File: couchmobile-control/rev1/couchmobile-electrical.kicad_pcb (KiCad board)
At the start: 2 copper layers, 100 x 100 mm, 54 parts, among them J1 Power_In, J10 Motor1, J11 Motor2, J2 GPIO_NANO_1, J5 ESTOP_IRQ_EN, J6 BNO_COMM_CTRL, J7 Conn_02x04_Top_Bottom, J8 Encoder1, J9 Encoder2, Q1 PMOS DGS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

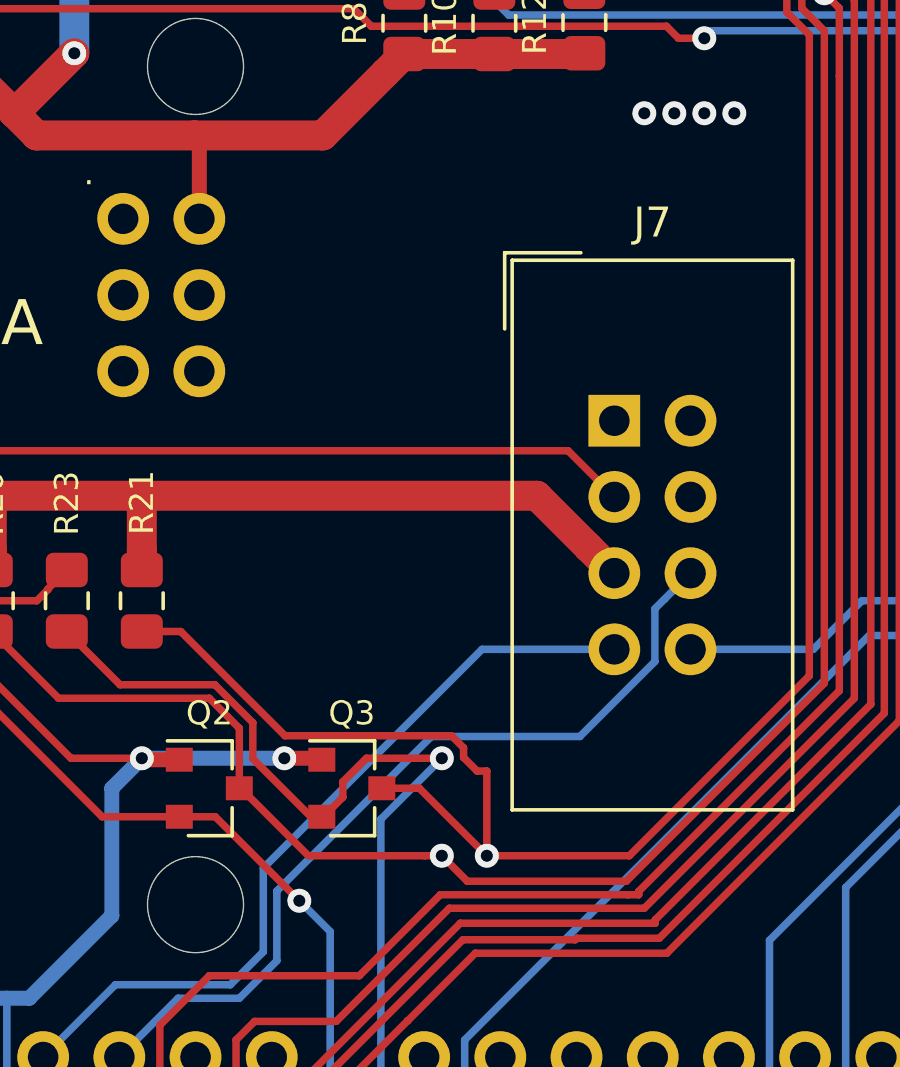
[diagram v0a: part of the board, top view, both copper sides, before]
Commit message: Added in label to control panel
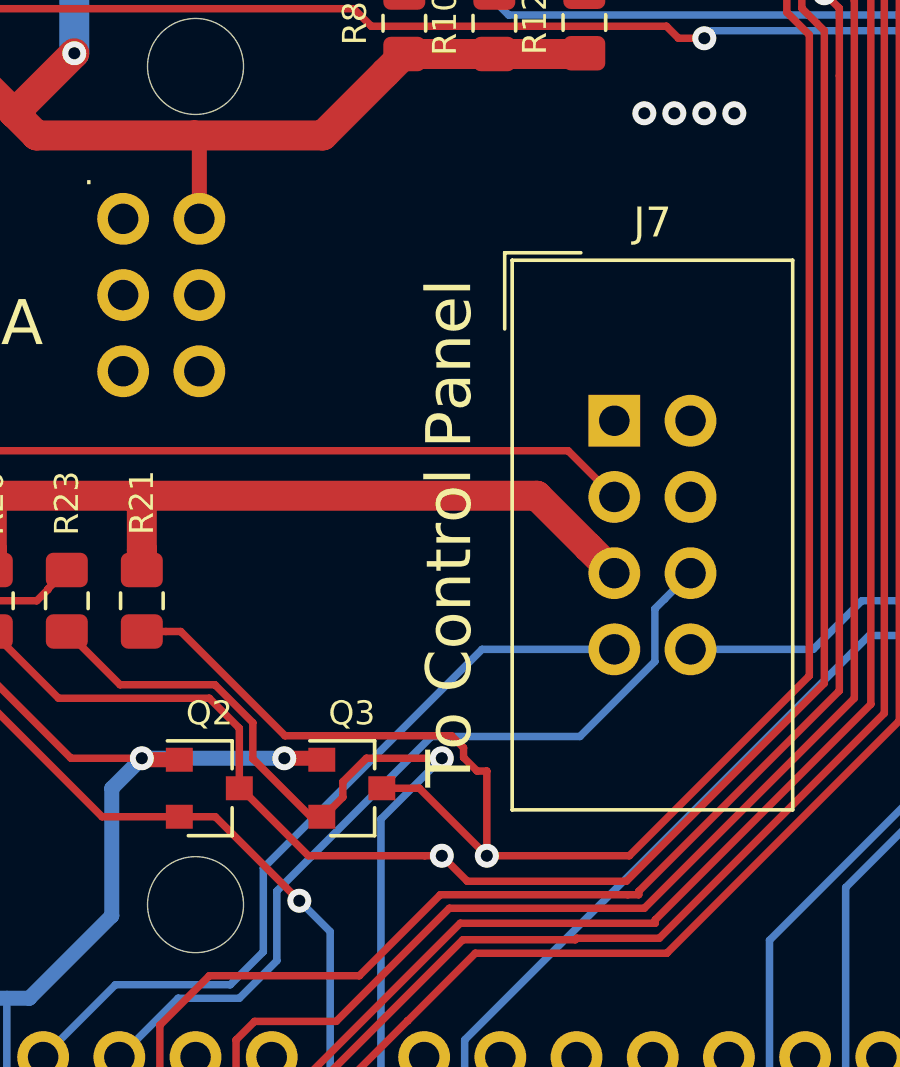
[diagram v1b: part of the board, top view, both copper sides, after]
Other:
- board text added: "To Control Panel"
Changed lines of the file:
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@@
   (general
     (thickness 1.6)
-    (drawings 36)
+    (drawings 37)
     (tracks 822)
     (zones 0)
@@
   )
   (setup
-    (last_trace_width 1)
+    (last_trace_width 0.25)
     (user_trace_width 0.25)
     (user_trace_width 0.5)
@@
     )
   )
+  (gr_text "To Control Panel" (at 94.5 54 90) (layer F.SilkS)
+    (effects (font (size 1.5 1.5) (thickness 0.3)))
+  )
   (gr_text "SPI SIDE" (at 93 99) (layer F.SilkS)
     (effects (font (size 1.5 1.5) (thickness 0.3)))
@@
   (segment (start 107.573002 36) (end 111.564401 32.008601) (width 0.25) (layer B.Cu) (net 3))
   (segment (start 107 36) (end 107.573002 36) (width 0.25) (layer B.Cu) (net 3))
+  (segment (start 88 107.975) (end 86.775 106.75) (width 0.25) (layer F.Cu) (net 3))
+  (segment (start 86.775 106.75) (end 84.91674 106.75) (width 0.25) (layer F.Cu) (net 3))
+  (segment (start 79.25 101.08326) (end 79.25 98.5) (width 0.25) (layer F.Cu) (net 3))
+  (segment (start 84.91674 106.75) (end 79.25 101.08326) (width 0.25) (layer F.Cu) (net 3))
+  (segment (start 79.25 98.79564) (end 79.25 98.5) (width 0.25) (layer F.Cu) (net 3))
+  (segment (start 79.25 98.5) (end 79.25 91.25) (width 0.25) (layer F.Cu) (net 3))
   (segment (start 88 110.025) (end 88 111.975) (width 0.25) (layer F.Cu) (net 4) (status 30))
   (segment (start 91 111.975) (end 91 110.025) (width 0.25) (layer F.Cu) (net 5) (status 30))
@@
   (segment (start 111.68 30.82) (end 113.98 30.82) (width 0.25) (layer B.Cu) (net 6) (status 20))
   (segment (start 107.5 35) (end 111.68 30.82) (width 0.25) (layer B.Cu) (net 6))
-  (segment (start 94 111.975) (end 94 110.025) (width 0.25) (layer F.Cu) (net 7) (status 30))
-  (segment (start 88 107.975) (end 86.775 106.75) (width 0.25) (layer F.Cu) (net 3))
-  (segment (start 86.775 106.75) (end 84.91674 106.75) (width 0.25) (layer F.Cu) (net 3))
-  (segment (start 79.25 101.08326) (end 79.25 98.5) (width 0.25) (layer F.Cu) (net 3))
-  (segment (start 84.91674 106.75) (end 79.25 101.08326) (width 0.25) (layer F.Cu) (net 3))
-  (segment (start 79.25 98.79564) (end 79.25 98.5) (width 0.25) (layer F.Cu) (net 3))
-  (segment (start 79.25 98.5) (end 79.25 91.25) (width 0.25) (layer F.Cu) (net 3))
   (segment (start 91 107.975) (end 89.275 106.25) (width 0.25) (layer F.Cu) (net 6))
   (segment (start 89.275 106.25) (end 85.25 106.25) (width 0.25) (layer F.Cu) (net 6))
@@
   (segment (start 80.025 98.93423) (end 80.025 98.75) (width 0.25) (layer F.Cu) (net 6))
   (segment (start 80.025 98.75) (end 80.025 92.082052) (width 0.25) (layer F.Cu) (net 6))
+  (segment (start 94 111.975) (end 94 110.025) (width 0.25) (layer F.Cu) (net 7) (status 30))
   (via (at 80.75 91.25) (size 0.8) (drill 0.4) (layers F.Cu B.Cu) (net 8))
   (segment (start 80.75 99.02282) (end 80.75 91.25) (width 0.25) (layer F.Cu) (net 8))
